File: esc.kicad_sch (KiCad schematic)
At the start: 4 parts, among them J1 Conn_01x02, J2 Screw_Terminal_01x01, J3 Screw_Terminal_01x01, J4 Screw_Terminal_01x01

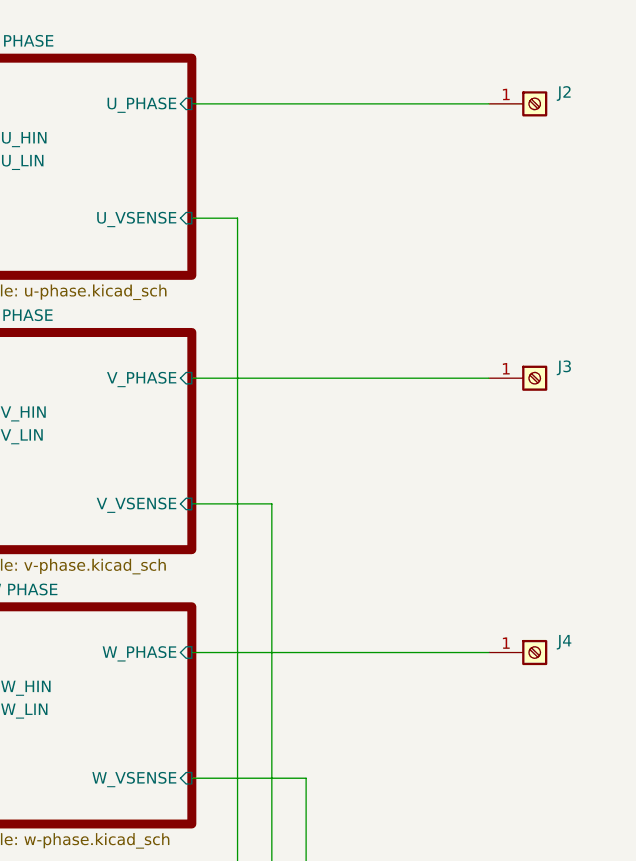
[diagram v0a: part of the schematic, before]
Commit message: completed layout -- DRC
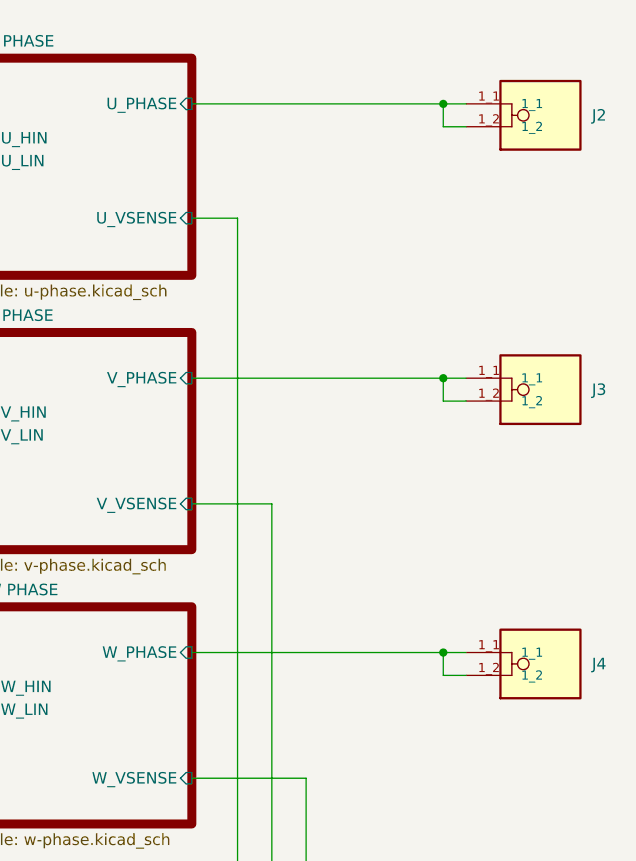
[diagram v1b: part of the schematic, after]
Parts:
- J2, J3, J4: footprint TerminalBlock_WAGO:TerminalBlock_WAGO_236-101_1x01_P5.00mm_45Degree -> esc-land-patterns:PHOENIX_1706701; symbol Connector:Screw_Terminal_01x01 -> ESC:1706701; MANUFACTURER (none) -> Phoenix Contact; MAXIMUM_PACKAGE_HEIGHT (none) -> 14.35mm; PARTREV (none) -> 24.09.2015; STANDARD (none) -> Manufacturer Recommendations
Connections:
- net U PHASE/U_PHASE: now also J2.1_1, J2.1_2; no longer J2.1 (Pin_1)
- net V PHASE/V_PHASE: now also J3.1_1, J3.1_2; no longer J3.1 (Pin_1)
- net W PHASE/W_PHASE: now also J4.1_1, J4.1_2; no longer J4.1 (Pin_1)
